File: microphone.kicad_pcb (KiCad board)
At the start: 2 copper layers, 16.9 x 17 mm, 9 parts, among them P1 BLC, P2 SB, P3 E, P4 PTT, P5 ME, P6 MIC, P7 HK, P8 DM

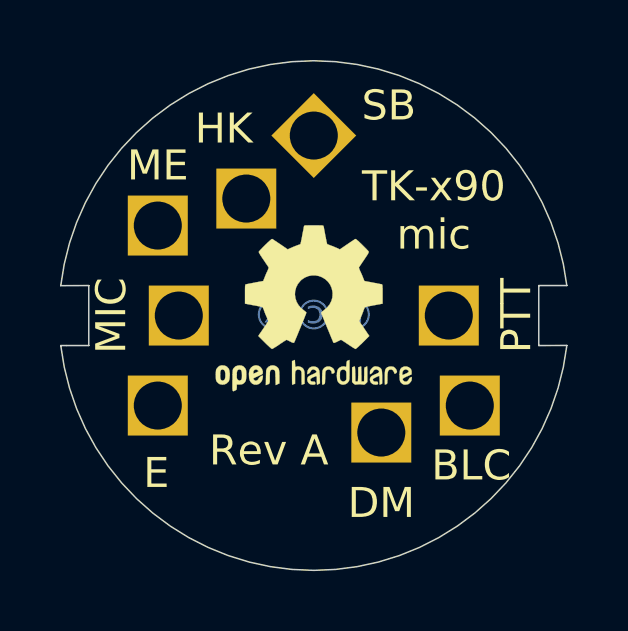
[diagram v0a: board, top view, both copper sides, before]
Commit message: Adds wirepads.
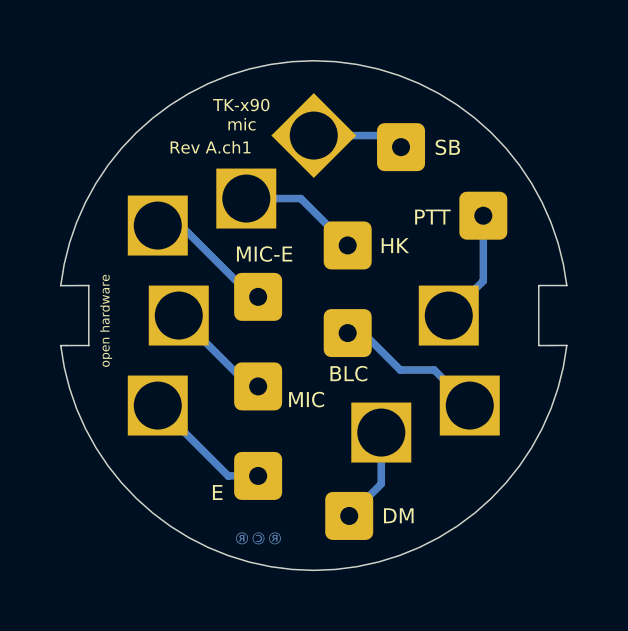
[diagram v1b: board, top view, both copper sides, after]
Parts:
- removed REF**: OSHW-Logo2_7.3x6mm_SilkScreen, Symbol:OSHW-Logo2_7.3x6mm_SilkScreen
- added J1: Conn_01x01, Connector_Wire:SolderWire-0.1sqmm_1x01_D0.4mm_OD1mm, F.Cu at (151.2, 106.7)
- added J2: Conn_01x01, Connector_Wire:SolderWire-0.1sqmm_1x01_D0.4mm_OD1mm, F.Cu at (151.1, 97.7)
- added J3: Conn_01x01, Connector_Wire:SolderWire-0.1sqmm_1x01_D0.4mm_OD1mm, F.Cu at (148.1, 102.4)
- added J4: Conn_01x01, Connector_Wire:SolderWire-0.1sqmm_1x01_D0.4mm_OD1mm, F.Cu at (148.1, 99.4)
- added J5: Conn_01x01, Connector_Wire:SolderWire-0.1sqmm_1x01_D0.4mm_OD1mm, F.Cu at (155.7, 96.7)
- added J6: Conn_01x01, Connector_Wire:SolderWire-0.1sqmm_1x01_D0.4mm_OD1mm, F.Cu at (148.1, 105.3)
- added J7: Conn_01x01, Connector_Wire:SolderWire-0.1sqmm_1x01_D0.4mm_OD1mm, F.Cu at (152.9, 94.4)
- added J8: Conn_01x01, Connector_Wire:SolderWire-0.1sqmm_1x01_D0.4mm_OD1mm, F.Cu at (151.1, 100.6)
- P5: value ME -> MIC-E
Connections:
- P1 pad 1: (no net) -> /BLC
- P2 pad 1: (no net) -> /SB
- P3 pad 1: (no net) -> /E
- P4 pad 1: (no net) -> /PTT
- P5 pad 1: (no net) -> /MIC-E
- P6 pad 1: (no net) -> /MIC
- P7 pad 1: (no net) -> /HK
- P8 pad 1: (no net) -> /DM
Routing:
- net /BLC: track 0.00 -> 5.07 mm
- net /MIC-E: track 0.00 -> 4.33 mm
- net /E: track 0.00 -> 4.32 mm
- net /HK: track 0.00 -> 4.03 mm
- net /PTT: track 0.00 -> 3.80 mm
- net /MIC: track 0.00 -> 3.62 mm
- net /DM: track 0.00 -> 3.22 mm
- net /SB: track 0.00 -> 3.07 mm
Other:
- board text added: "BLC"
- board text added: "DM"
- board text added: "E"
- board text added: "HK"
- board text added: "MIC"
- board text added: "MIC-E"
- board text added: "PTT"
- board text added: "Rev A.ch1"
- board text added: "SB"
- board text added: "open hardware"
- board text removed: "Rev A"
